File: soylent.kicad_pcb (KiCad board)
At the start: 2 copper layers, 34.5 x 43.2 mm, 33 parts, among them J1 DB9_Female, J2 Conn_01x04, J3 Conn_01x04, J4 Conn_02x03_Counter_Clockwise, Q1 BC847, Q3 BC847BPN, U1 ATtiny202-SS, U2 MIC5504-3.3YM5, U3 LM2776, U4 MAX3188EEUT+T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

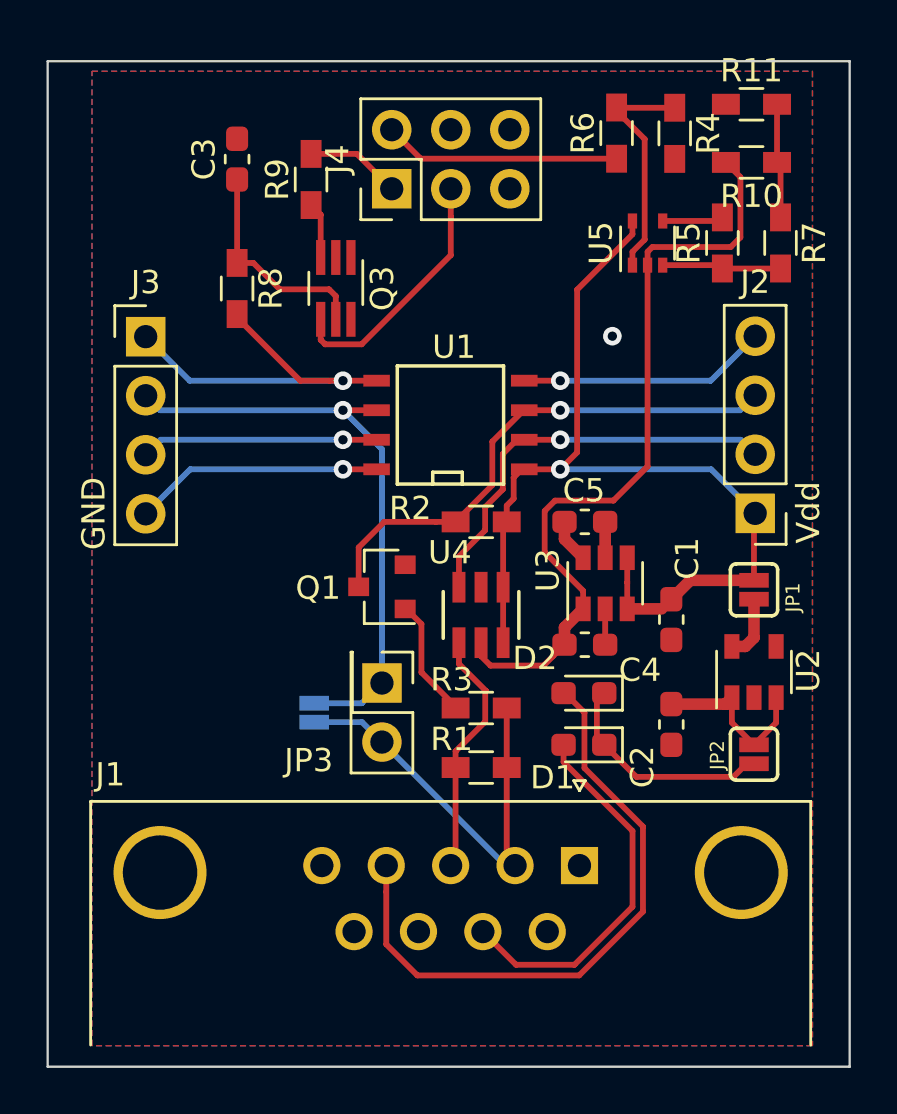
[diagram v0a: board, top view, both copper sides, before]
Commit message: Shrink cut lines
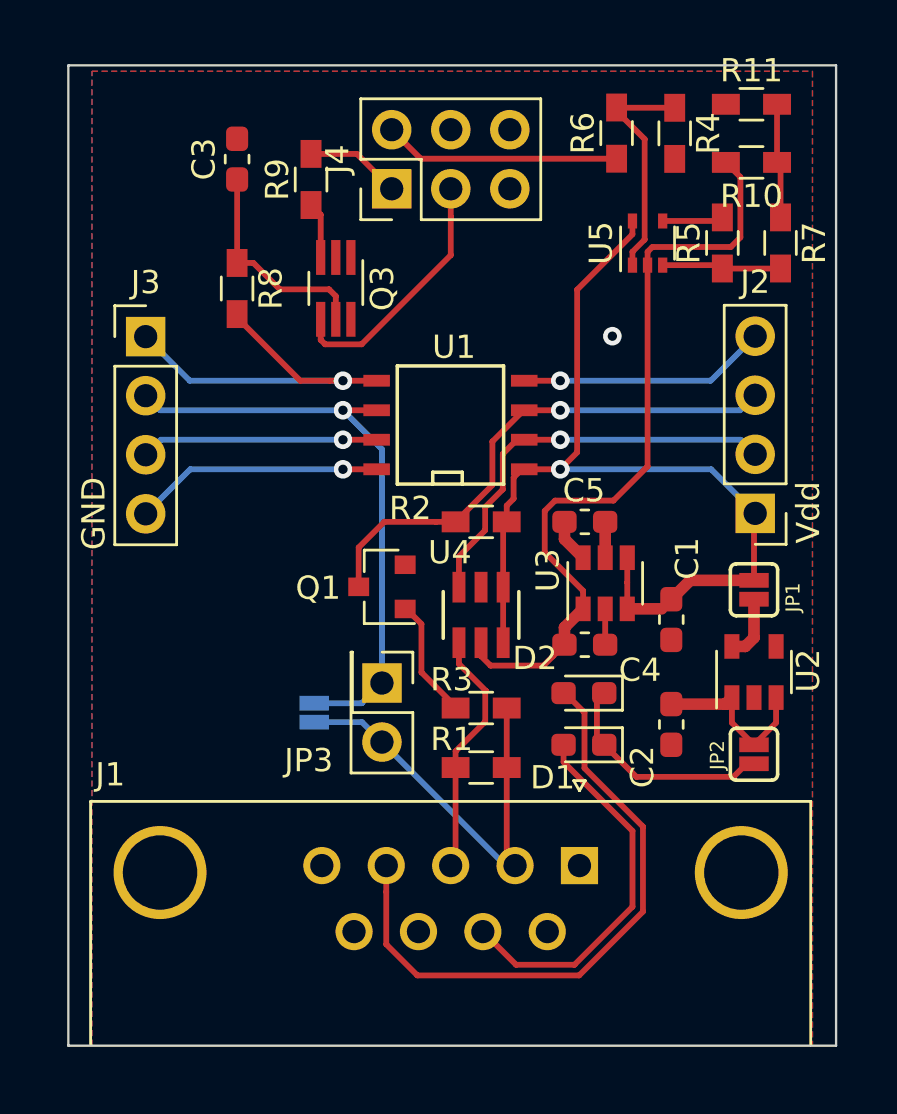
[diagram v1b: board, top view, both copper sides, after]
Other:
- board size 34.5 x 43.2 mm -> 33 x 42.2 mm
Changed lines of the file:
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@@
     )
   )
-  (gr_line (start 221.8944 63.008) (end 221.8944 19.7612) (layer Edge.Cuts) (width 0.1))
-  (gr_line (start 256.3876 63.008) (end 221.8944 63.008) (layer Edge.Cuts) (width 0.1))
-  (gr_line (start 256.3876 19.7612) (end 256.3876 63.008) (layer Edge.Cuts) (width 0.1))
-  (gr_line (start 221.8944 19.7612) (end 256.3876 19.7612) (layer Edge.Cuts) (width 0.1))
+  (gr_line (start 222.7834 62.103) (end 222.7834 19.939) (layer Edge.Cuts) (width 0.1))
+  (gr_line (start 255.8034 62.103) (end 222.7834 62.103) (layer Edge.Cuts) (width 0.1))
+  (gr_line (start 255.8034 19.939) (end 255.8034 62.103) (layer Edge.Cuts) (width 0.1))
+  (gr_line (start 222.7834 19.939) (end 255.8034 19.939) (layer Edge.Cuts) (width 0.1))
   (gr_text Vdd (at 254.6096 39.1668 90) (layer F.SilkS)
     (effects (font (size 1 1) (thickness 0.25)))

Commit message: Arbitrary rerouting in search of a cure
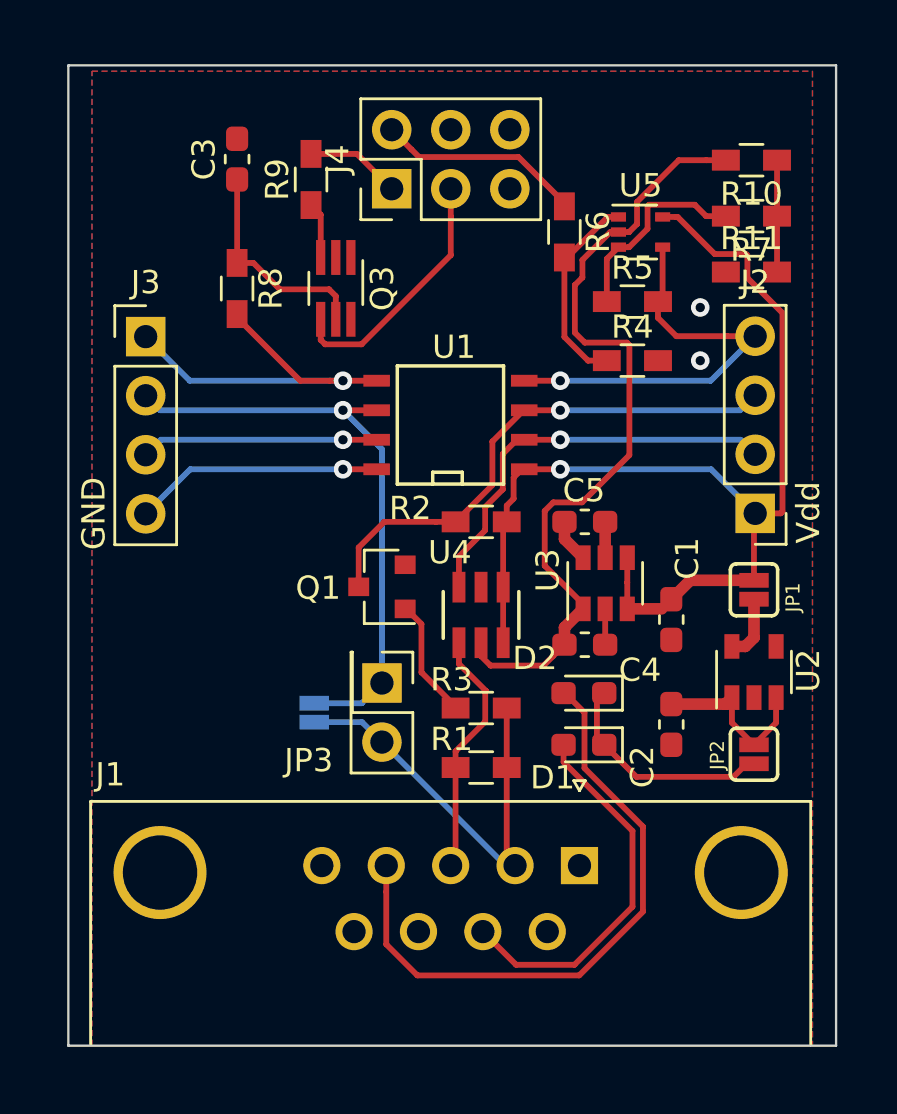
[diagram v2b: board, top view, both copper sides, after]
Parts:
- moved R4 9.94 mm to (247.0, 32.6), turned to 0 degrees
- moved R11 7.22 mm to (252.2, 28.8)
- moved R6 4.81 mm to (244.1, 27.1), turned to 270 degrees
- moved R5 4.62 mm to (247.0, 30.1), turned to 0 degrees
- moved R7 1.70 mm to (252.2, 26.4), turned to 180 degrees
- moved U5 0.56 mm to (247.4, 27.1), turned to 0 degrees
- moved R10 0.09 mm to (252.2, 24.0)
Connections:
- R5 pad 2: Net-(R5-Pad2) -> /WIN
- U5 pad 4: Net-(R5-Pad2) -> /WIN
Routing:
- net /WIN: track 10.7 -> 18.4 mm
- net VDD: track 41.6 -> 46.8 mm
- net Net-(R5-Pad1): track 5.13 -> 8.91 mm
- net Net-(R5-Pad2): track 2.63 -> 0.00 mm
- net VEE: track 33.7 -> 35.1 mm
- net Net-(J4-Pad2): track 10.2 -> 8.88 mm
- net Net-(R4-Pad1): track 10.0 -> 8.71 mm
- net GND: vias 2 -> 3

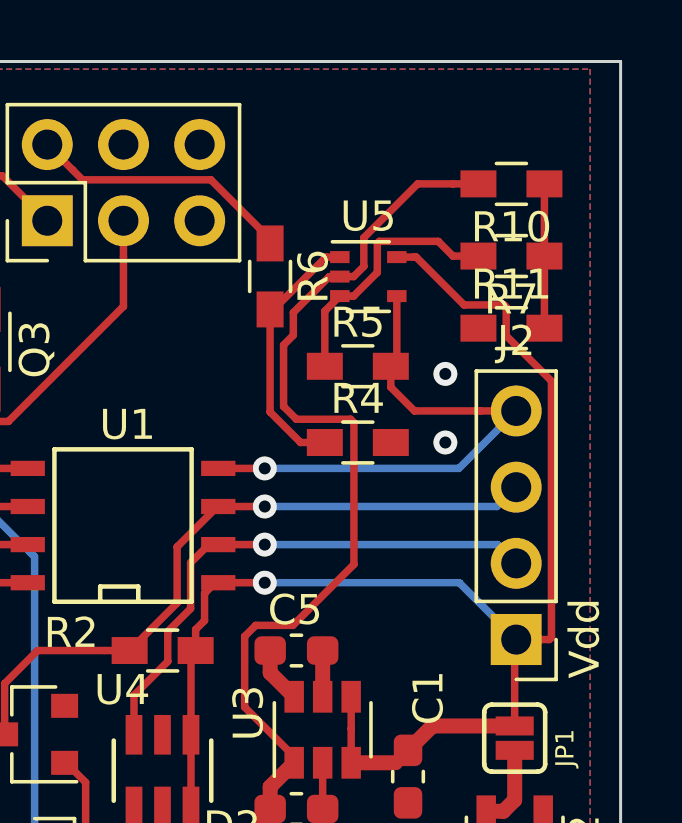
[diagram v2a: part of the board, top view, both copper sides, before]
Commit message: Inline a voltage divider into op-amp feedback
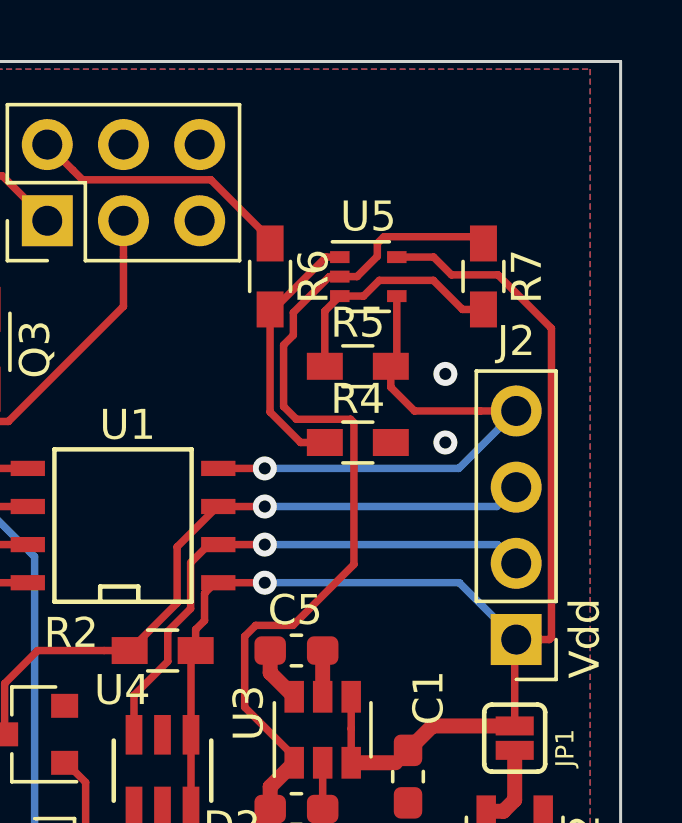
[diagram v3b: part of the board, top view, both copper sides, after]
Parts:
- removed R10, R11: 10k, Resistors_SMD:R_0603_HandSoldering
- R7: value 50k -> 150k
- moved R7 1.15 mm to (251.2, 27.1), turned to 270 degrees
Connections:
- R7 pad 1: Net-(R10-Pad1) -> VEE
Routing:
- net Net-(R10-Pad1): track 5.02 -> 0.00 mm
- net Net-(R5-Pad1): track 8.91 -> 7.95 mm
- net VEE: track 35.1 -> 34.3 mm

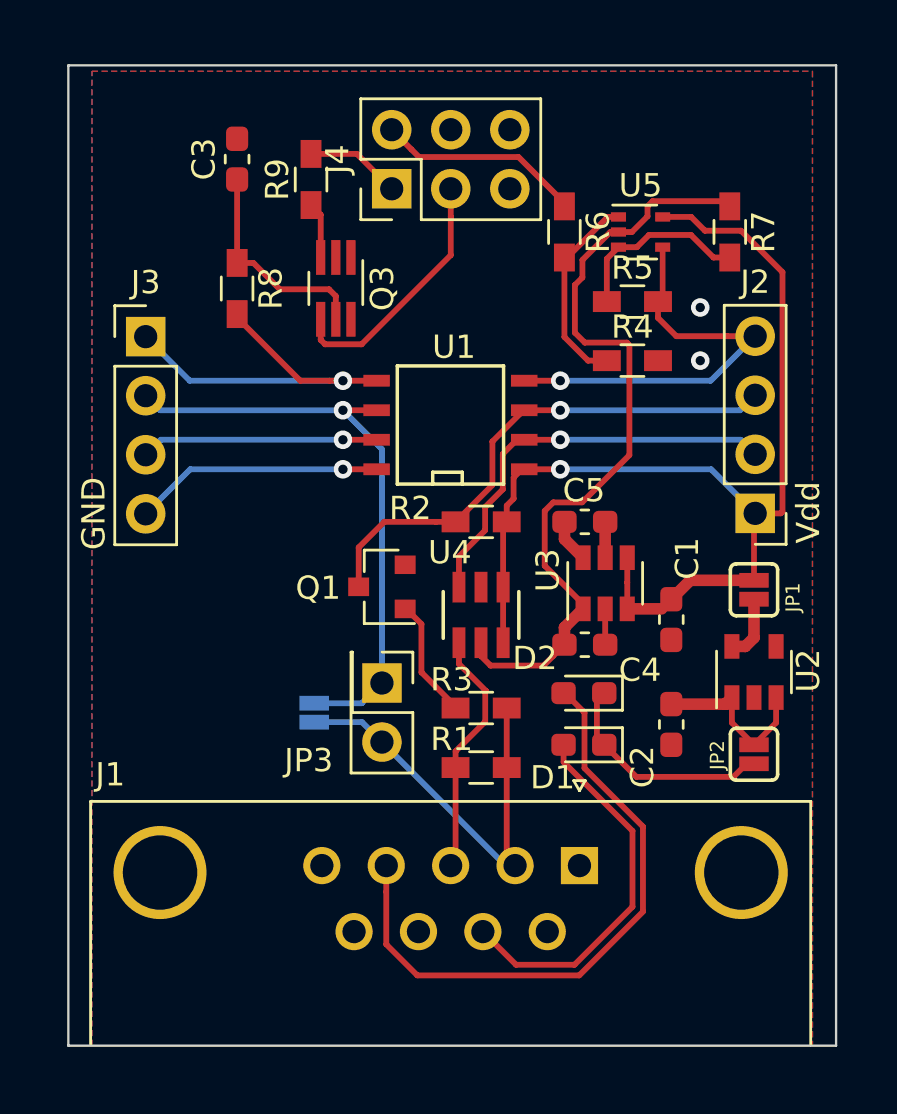
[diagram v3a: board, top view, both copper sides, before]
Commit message: Fit into a smaller space
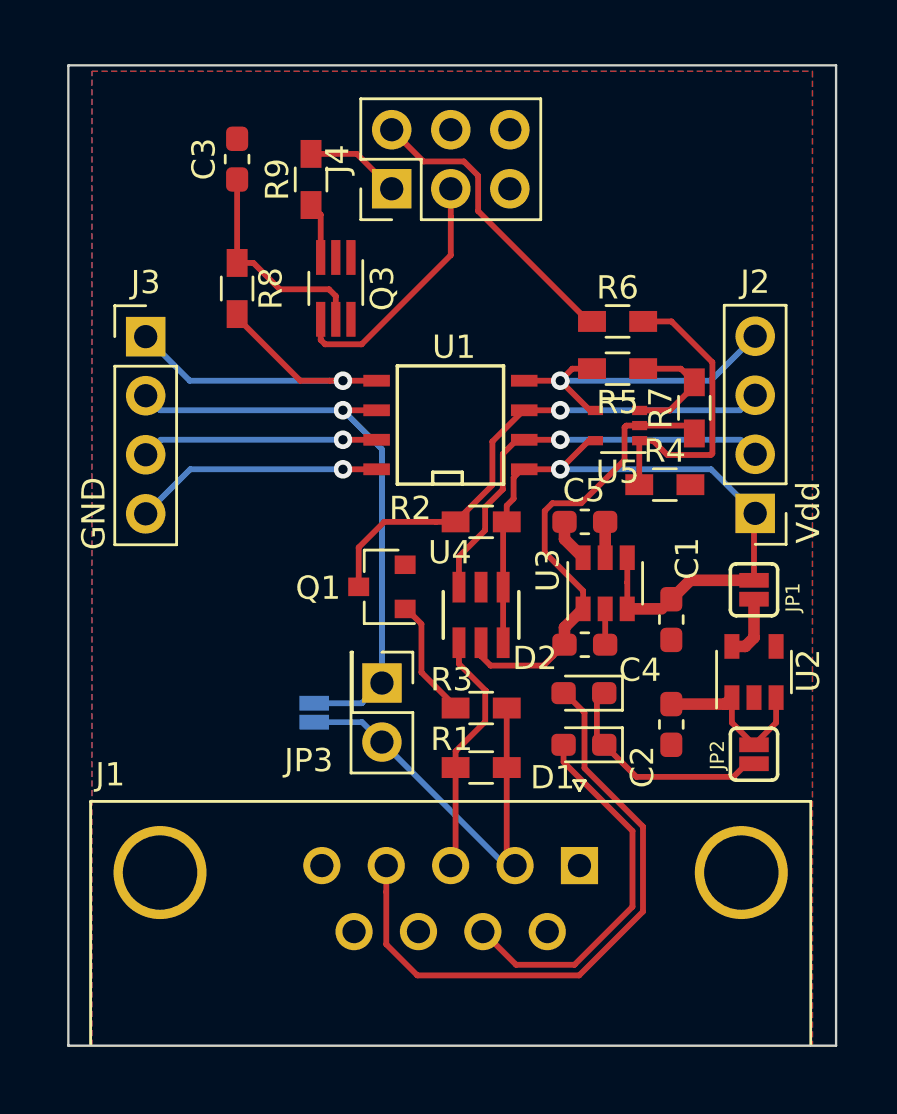
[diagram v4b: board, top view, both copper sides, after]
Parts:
- moved U5 8.38 mm to (246.4, 35.4), turned to 180 degrees
- moved R7 7.72 mm to (249.7, 34.7), turned to 90 degrees
- moved R4 5.51 mm to (248.4, 38.0)
- moved R6 4.48 mm to (246.4, 31.0), turned to 0 degrees
- moved R5 2.96 mm to (246.4, 33.0), turned to 180 degrees
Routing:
- net VDD: track 47.3 -> 31.7 mm
- net VEE: track 34.3 -> 20.4 mm
- net Net-(R4-Pad1): track 8.71 -> 12.9 mm
- net Net-(J4-Pad2): track 8.88 -> 12.9 mm
- net /WIN: track 18.4 -> 14.3 mm
- net Net-(R5-Pad1): track 7.95 -> 5.39 mm
- net GND: vias 3 -> 1

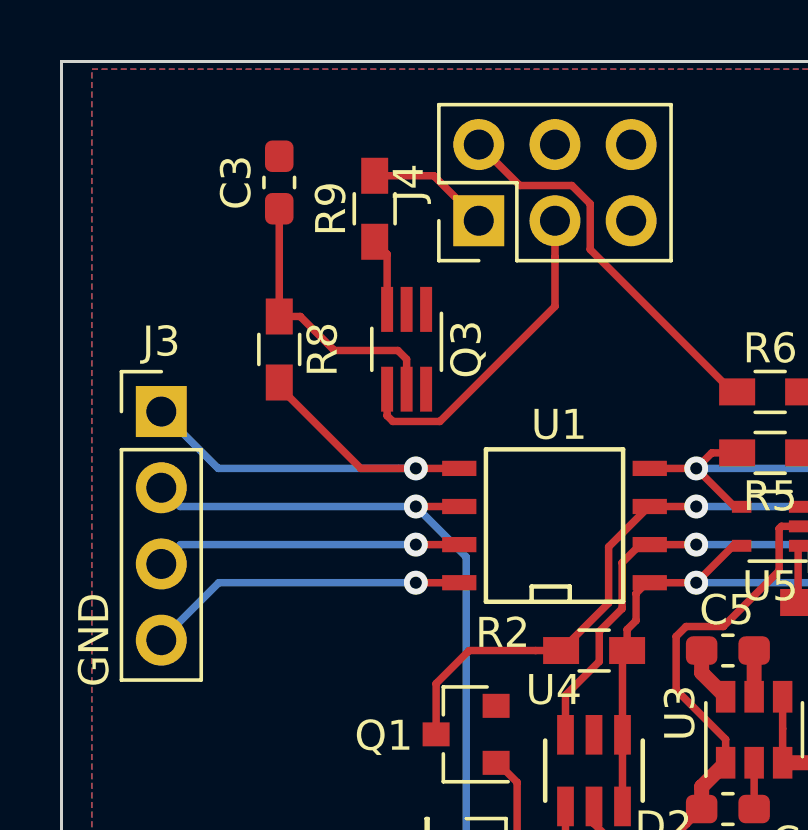
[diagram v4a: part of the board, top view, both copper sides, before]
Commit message: Shrink and move filter/driver
Fix a bug with an inadvertent connection to RX from WIN, too
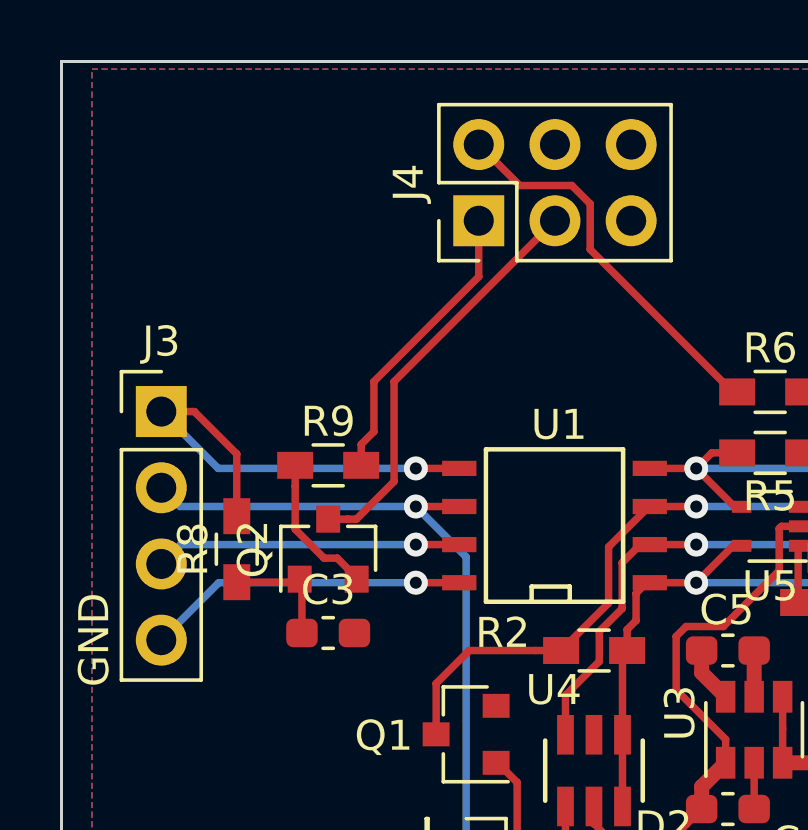
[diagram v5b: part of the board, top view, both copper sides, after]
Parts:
- removed Q3: BC847BPN, TO_SOT_Packages_SMD:SOT-363_SC-70-6_Handsoldering
- added Q2: BC847, Package_TO_SOT_SMD:SOT-23, F.Cu at (231.7, 36.2)
- moved C3 15.1 mm to (231.7, 39.0), turned to 0 degrees
- moved R9 8.69 mm to (231.7, 33.4), turned to 0 degrees
- moved R8 6.81 mm to (228.6, 36.2), turned to 90 degrees
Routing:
- net Net-(J4-Pad1): track 4.09 -> 9.78 mm
- net Net-(C3-Pad1): track 9.43 -> 3.96 mm
- net Net-(J4-Pad3): track 11.0 -> 13.6 mm
- net Net-(Q2-Pad2): track 2.43 -> 4.90 mm
- net /WOUT: track 16.5 -> 15.9 mm
